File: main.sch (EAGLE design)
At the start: 474 parts, among them J100 DCJ0202, Q200 NMOS, Q201 PMOS, Q300 PMOS, Q400 PMOS, U100 NE555N, U1000 74LS173N, U1001 74LS173N, U1002 74LS245N, U1003 74LS173N, U1004 74LS173N, U1005 74LS245N, U101 NE555N, U102 NE555N, U103 74LS04N, U104 74LS08N, U105 74LS32N, U1100 74LS173N, U1101 74LS173N, U1102 74LS161N, U1106 74HCT154DW, U1107 74HCT154DW, U1108 74LS04N, U1109 74LS04N, U200 HM62256, U201 74LS173N, U202 74LS173N, U203 74LS173N, U204 74LS173N, U205 74LS157N, U206 74LS157N, U207 74LS157N, U208 74LS157N, U209 74HCT595D, U210 74HCT595D, U211 74HCT595D, U212 74LS245N, U213 74LS245N, U214 74LS00N, U215 74LS173N, U216 74LS173N, U217 74LS173N, U218 74LS173N, U219 74LS245N, U220 74LS245N, U300 74LS299N, U301 74LS245N, U302 74LS08N, U303 74LS00N, U304 74LS245N, U400 74LS00N, U401 74LS245N, U500 74LS161N, U501 74LS161N, U502 74LS161N, U503 74LS161N, U504 74LS245N, U505 74LS245N, U600 74LS173N, U601 74LS173N, U602 74LS173N, U603 74LS173N, U604 74LS245N, U700 74LS283N, U701 74LS283N, U702 74LS245N, U703 74LS86N, U704 74LS86N, U705 74LS85N, U706 74LS85N, U707 74LS173N, U708 74LS125N, U800 74LS04N, U801 74LS04N, U802 74LS08N, U803 74LS08N, U804 74LS32N, U805 74LS32N, U806 74LS86N, U807 74LS86N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

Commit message: Routing and layout done.
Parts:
- removed C1109: 0.1µF, rcl:C-EUC0805K
- removed U1109: 74LS04N, 74xx-us:74LS04N
- added C709: 0.1µF, rcl:C-EUC0805K
- added J400: 90152-12, 8BitCpuParts:90152-12
- added LED401: (no value), led:LEDCHIP-LED0805
- added Q401, Q402: NMOS, ExtraParts:SOT23-N-MOSFET
- added R1103: 330Ω?, resistor:R-US_R0805
- added R403: 10kΩ, resistor:R-US_R0805
- added R404: 1kΩ, resistor:R-US_R0805
- added S402: NK236H, 8BitCpuParts:NK236H
- added U709: 74LS153N, 74xx-us:74LS153N
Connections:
- net CMP_= renamed CMP_EQ_INT
- removed net CMP_<: U706A.A<B_O, U707A.D1
- removed net CMP_>: U706A.A>B_O, U707A.D3
- removed net CTRL_15: LED1164.A, XU1105A.D7
- removed net OUT_15: U1108D.O
- new net CMP_GT_INT: U707A.D3, U709A.2Y
- new net CMP_GT_PRE: U706A.A>B_O, U709A.1C3, U709A.2C0, U709A.2C1, U709A.2C2
- new net CMP_LT_INT: U707A.D1, U709A.1Y
- new net CMP_LT_PRE: U706A.A<B_O, U709A.1C0, U709A.1C1, U709A.1C2, U709A.2C3
- new net CPTC: LED1153.A, U709A.B, XU1104A.D4
- new net INPUT_GND: Q401.D, S400.10, S400.11, S400.12, S400.13, S400.14, S400.15, S400.16, S400.9
- new net INPUT_GND_INT: Q401.S, Q402.D
- new net INPUT_LOCK_ARDUINO: A200.A4, Q401.G, R403.1
- new net INPUT_LOCK_EXT: LED401.C, Q402.G, S402.P
- new net LED401_VCC: LED401.A, R404.2
- net !CLK: now also U800F.O
- net !CMP: now also U800A.O; no longer U1109A.O
- net !FE: now also U1108E.O; no longer U1109B.O
- net !NO: now also A200.D8, J400.3
- net !OUT_15: no longer U1108D.I
- net !RM: now also U1108C.O; no longer U1109C.O
- net !RMSB: now also U1108D.O; no longer U1109D.O
- net !RO: now also U1108F.I; no longer U1108C.I
- net BITWISE_XOR_7: now also U709A.A
- net CLK: now also U800F.I
- net CMP: now also U800A.I; no longer U1109A.I
- net FE: now also LED1154.A, U1108E.I, XU1104A.D5; no longer LED1153.A, U1109B.I, XU1104A.D4
- net GND: now also C709.2, J400.1, Q402.S, R1103.2, S402.S, U709A.1G, U709A.2G; no longer C1109.2, S400.10, S400.11, S400.12, S400.13, S400.14, S400.15, S400.16, S400.9
- net HLT: now also LED1155.A, XU1104A.D6; no longer LED1154.A, XU1104A.D5
- net INPUT_0: now also A200.D9, J400.5
- net INPUT_1: now also A200.D10, J400.7
- net INPUT_2: now also A200.D11, J400.9
- net INPUT_3: now also A200.D12, J400.11
- net INPUT_4: now also A200.A0, J400.6
- net INPUT_5: now also A200.A1, J400.8
- net INPUT_6: now also A200.A2, J400.10
- net INPUT_7: now also A200.A3, J400.12
- net LED1107_GND: now also R1100.1; no longer RN1100.R8_1
- net LED1108_GND: now also R1101.1; no longer R1100.1
- net LED1109_GND: now also R1102.1; no longer R1101.1
- net LED1110_GND: now also R1103.1; no longer R1102.1
- net LED1111_GND: now also RN1101.R8_1; no longer RN1101.R1_1
- net LED1112_GND: now also RN1101.R7_1; no longer RN1101.R2_1
- net LED1113_GND: now also RN1101.R6_1; no longer RN1101.R3_1
- net LED1114_GND: now also RN1101.R5_1; no longer RN1101.R4_1
- net LED1115_GND: now also RN1101.R4_1; no longer RN1101.R5_1
- net LED1116_GND: now also RN1101.R3_1; no longer RN1101.R6_1
- net LED1117_GND: now also RN1101.R2_1; no longer RN1101.R7_1
- net LED1118_GND: now also RN1101.R1_1; no longer RN1101.R8_1
- net LED1134_VCC: now also RN1104.R7_1; no longer RN1104.R2_1
- net LED1135_VCC: now also RN1104.R6_1; no longer RN1104.R3_1
- net LED1136_VCC: now also RN1104.R5_1; no longer RN1104.R4_1
- net LED1137_VCC: now also RN1104.R4_1; no longer RN1104.R5_1
- net LED1138_VCC: now also RN1104.R3_1; no longer RN1104.R6_1
- net LED1139_VCC: now also RN1104.R2_1; no longer RN1104.R7_1
- net LED1140_VCC: now also RN1104.R1_1; no longer RN1104.R8_1
- net LED1141_VCC: now also RN1105.R8_1; no longer RN1105.R1_1
- net LED1142_VCC: now also RN1105.R7_1; no longer RN1105.R2_1
- net LED1143_VCC: now also RN1105.R6_1; no longer RN1105.R3_1
- net LED1144_VCC: now also RN1105.R5_1; no longer RN1105.R4_1
- net LED1145_VCC: now also RN1105.R4_1; no longer RN1105.R5_1
- net LED1146_VCC: now also RN1105.R3_1; no longer RN1105.R6_1
- net LED1147_VCC: now also RN1105.R2_1; no longer RN1105.R7_1
- net LED1148_VCC: now also RN1105.R1_1; no longer RN1105.R8_1
- net LED1149_GND: now also RN1106.R8_1; no longer RN1106.R1_1
- net LED1150_GND: now also RN1106.R7_1; no longer RN1106.R2_1
- net LED1151_GND: now also RN1106.R6_1; no longer RN1106.R3_1
- net LED1152_GND: now also RN1106.R5_1; no longer RN1106.R4_1
- net LED1153_GND: now also RN1106.R4_1; no longer RN1106.R5_1
- net LED1154_GND: now also RN1106.R3_1; no longer RN1106.R6_1
- net LED1155_GND: now also RN1106.R2_1; no longer RN1106.R7_1
- net LED1156_GND: now also RN1106.R1_1; no longer RN1106.R8_1
- net LED1157_GND: now also RN1107.R8_1; no longer RN1107.R1_1
- net LED1158_GND: now also RN1107.R7_1; no longer RN1107.R2_1
- net LED1159_GND: now also RN1107.R6_1; no longer RN1107.R3_1
- net LED1160_GND: now also RN1107.R5_1; no longer RN1107.R4_1
- net LED1161_GND: now also RN1107.R4_1; no longer RN1107.R5_1
- net LED1162_GND: now also RN1107.R3_1; no longer RN1107.R6_1
- net LED1163_GND: now also RN1107.R2_1; no longer RN1107.R7_1
- net LED1164_GND: now also RN1107.R1_1; no longer RN1107.R8_1
- net NO_RESET_PULSE: now also A200.D7, J400.4
- net RM: now also LED1156.A, U1108C.I, XU1104A.D7; no longer LED1155.A, U1109C.I, XU1104A.D6
- net RMSB: now also LED1157.A, U1108D.I, XU1105A.D0; no longer LED1156.A, U1109D.I, XU1104A.D7
- net RO: now also U1108F.O; no longer U1108C.O
- net SM0: now also LED1158.A, XU1105A.D1; no longer LED1157.A, XU1105A.D0
- net SM1: now also LED1159.A, XU1105A.D2; no longer LED1158.A, XU1105A.D1
- net SRO: now also LED1160.A, XU1105A.D3; no longer LED1159.A, XU1105A.D2
- net SUB: now also LED1161.A, XU1105A.D4; no longer LED1160.A, XU1105A.D3
- net T0: now also LED1162.A, XU1105A.D5; no longer LED1161.A, XU1105A.D4
- net T1: now also LED1163.A, XU1105A.D6; no longer LED1162.A, XU1105A.D5
- net VCC: now also C709.1, J400.2, R403.2, R404.1, S402.O; no longer C1109.1
- net XR: now also LED1164.A, XU1105A.D7; no longer LED1163.A, XU1105A.D6

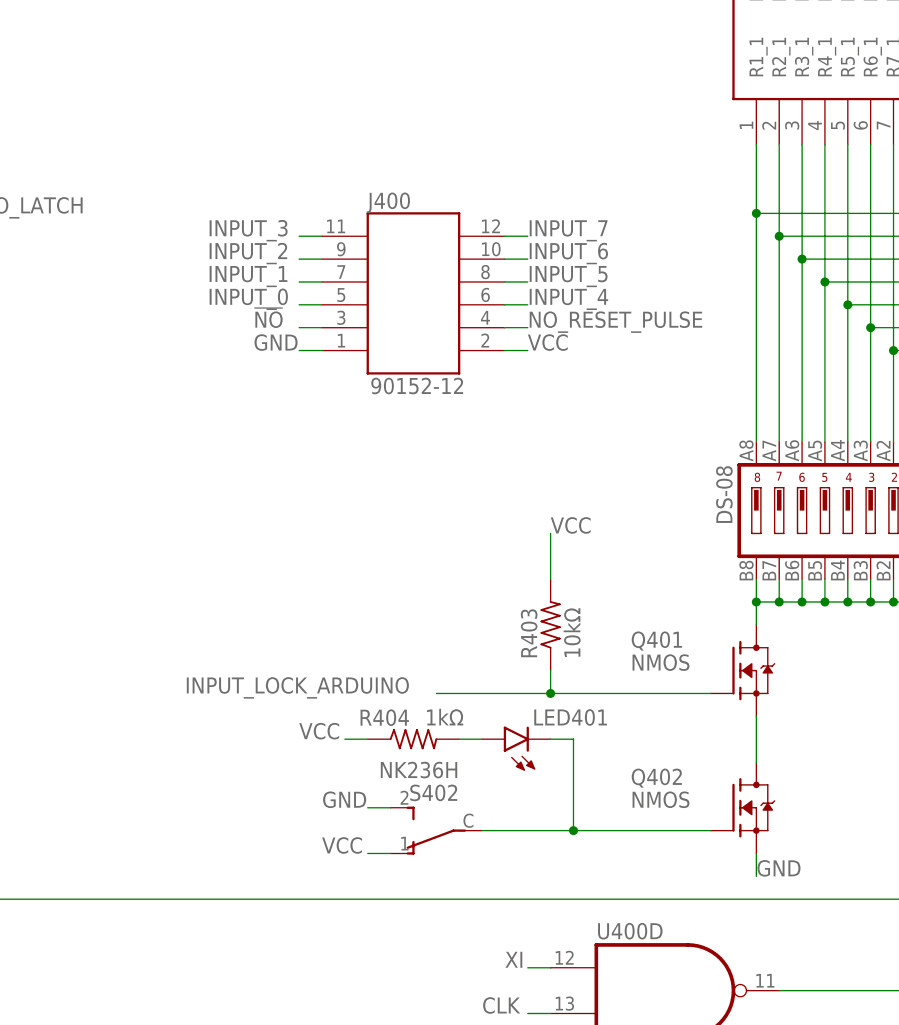
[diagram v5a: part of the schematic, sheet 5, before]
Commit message: Revised external input, progress on silkscreen.
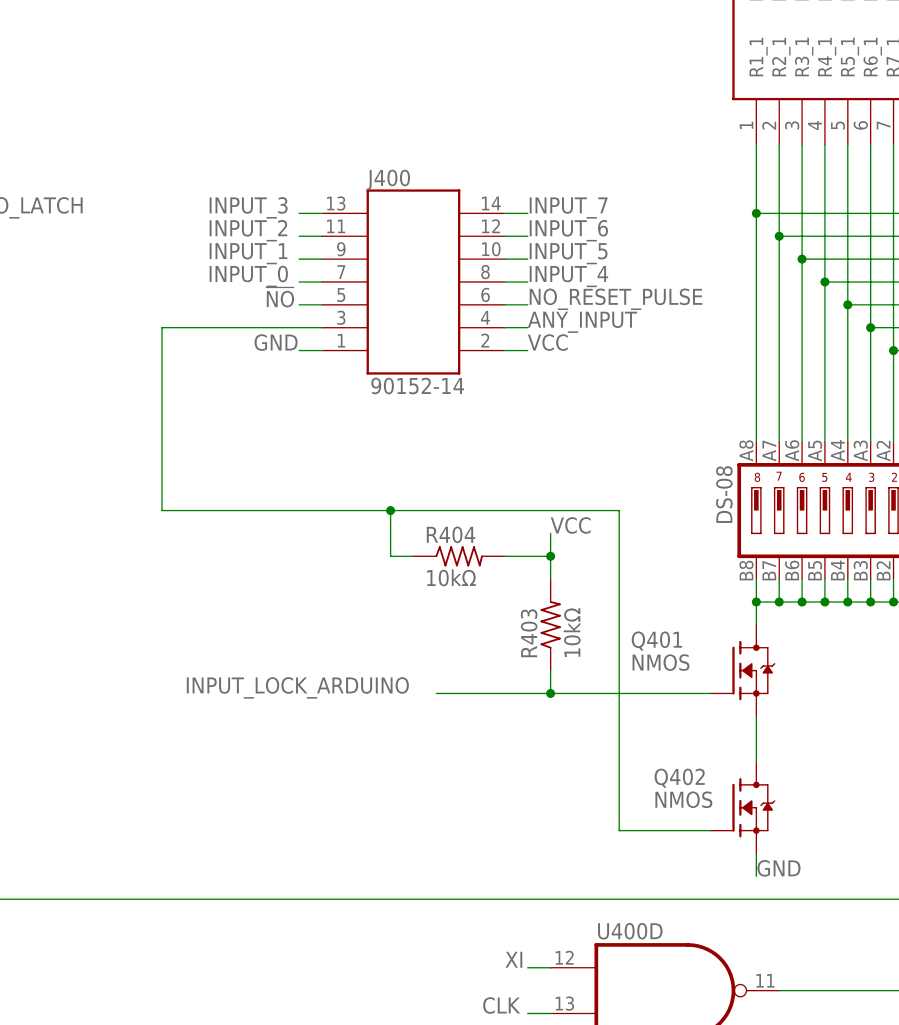
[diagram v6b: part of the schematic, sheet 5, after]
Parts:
- removed LED401: (no value), led:LEDCHIP-LED0805
- removed S402: NK236H, 8BitCpuParts:NK236H
- J400: value 90152-12 -> 90152-14; device 8BitCpuParts:90152-12 -> 8BitCpuParts:90152-14
- R404: value 1kΩ -> 10kΩ
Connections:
- removed net LED401_VCC: LED401.A, R404.2
- new net ANY_INPUT: A200.A5, J400.4, U1106A.0
- net !NO: now also J400.5; no longer J400.3
- net GND: no longer S402.S
- net INPUT_0: now also J400.7; no longer J400.5
- net INPUT_1: now also J400.9; no longer J400.7
- net INPUT_2: now also J400.11; no longer J400.9
- net INPUT_3: now also J400.13; no longer J400.11
- net INPUT_4: now also J400.8; no longer J400.6
- net INPUT_5: now also J400.10; no longer J400.8
- net INPUT_6: now also J400.12; no longer J400.10
- net INPUT_7: now also J400.14; no longer J400.12
- net INPUT_LOCK_EXT: now also J400.3, R404.1; no longer LED401.C, S402.P
- net NO_RESET_PULSE: now also J400.6; no longer J400.4
- net VCC: now also R404.2; no longer R404.1, S402.O
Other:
- moved on the sheet: R404

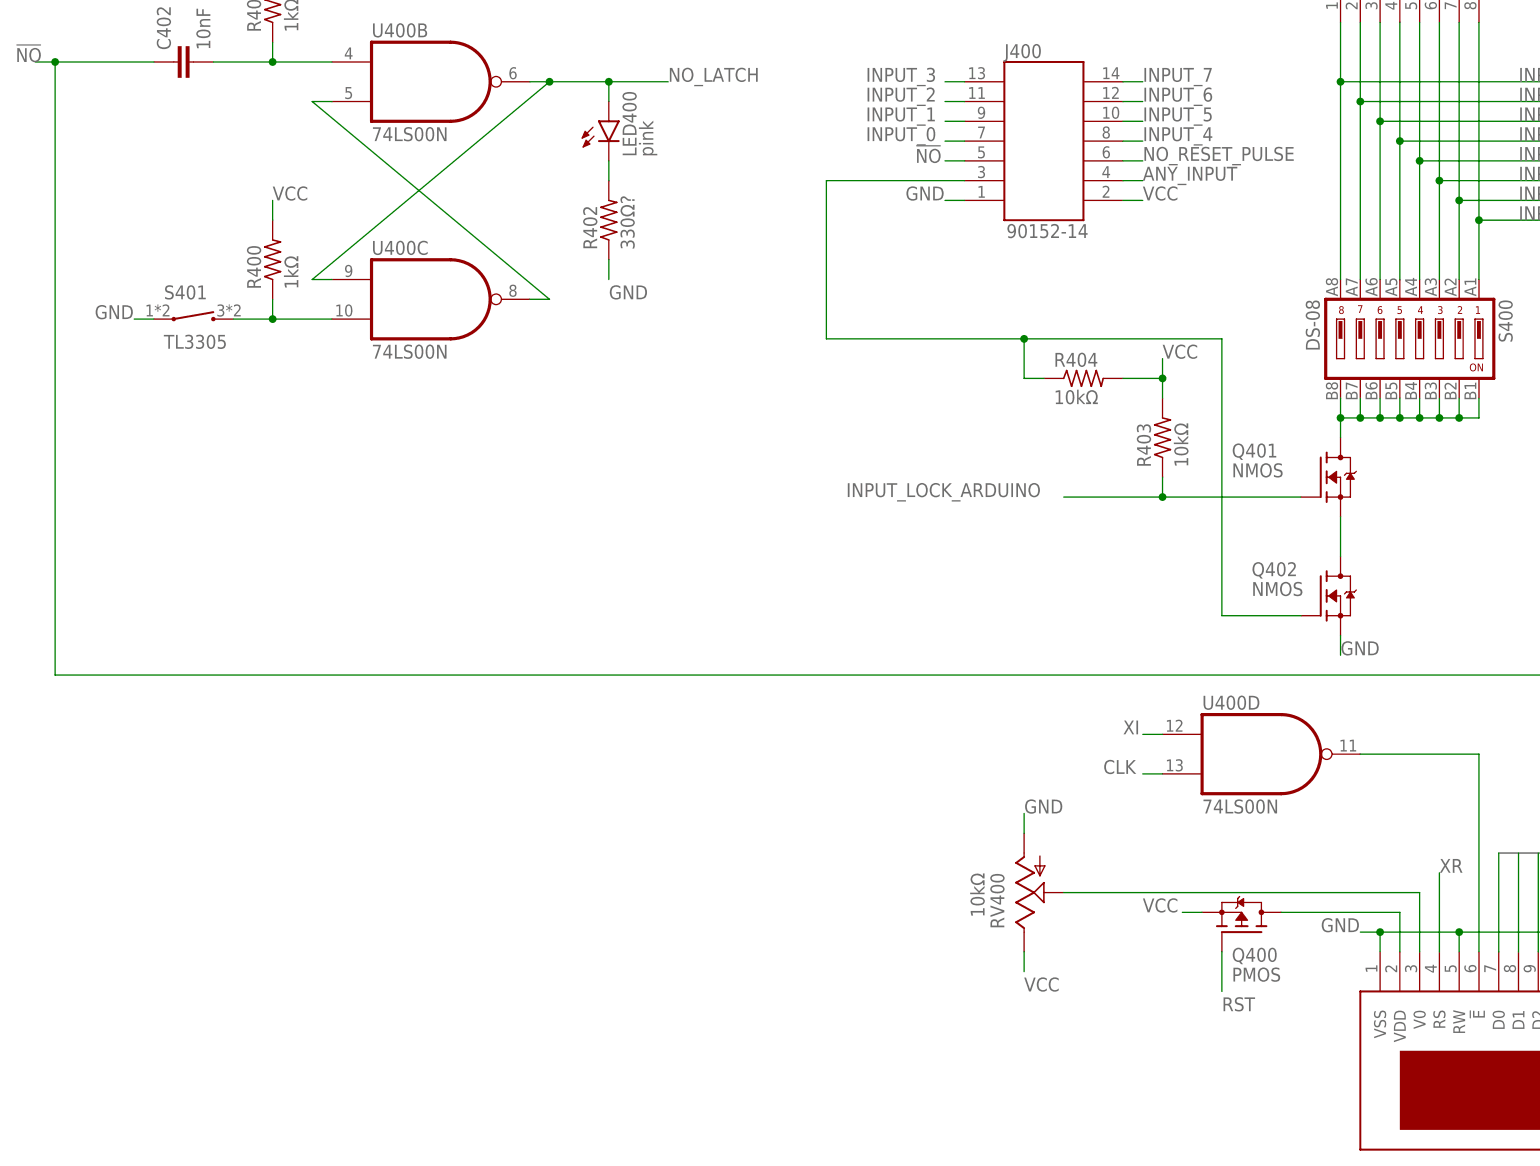
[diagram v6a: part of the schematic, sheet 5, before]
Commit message: Fixed issues encountered during build and testing.
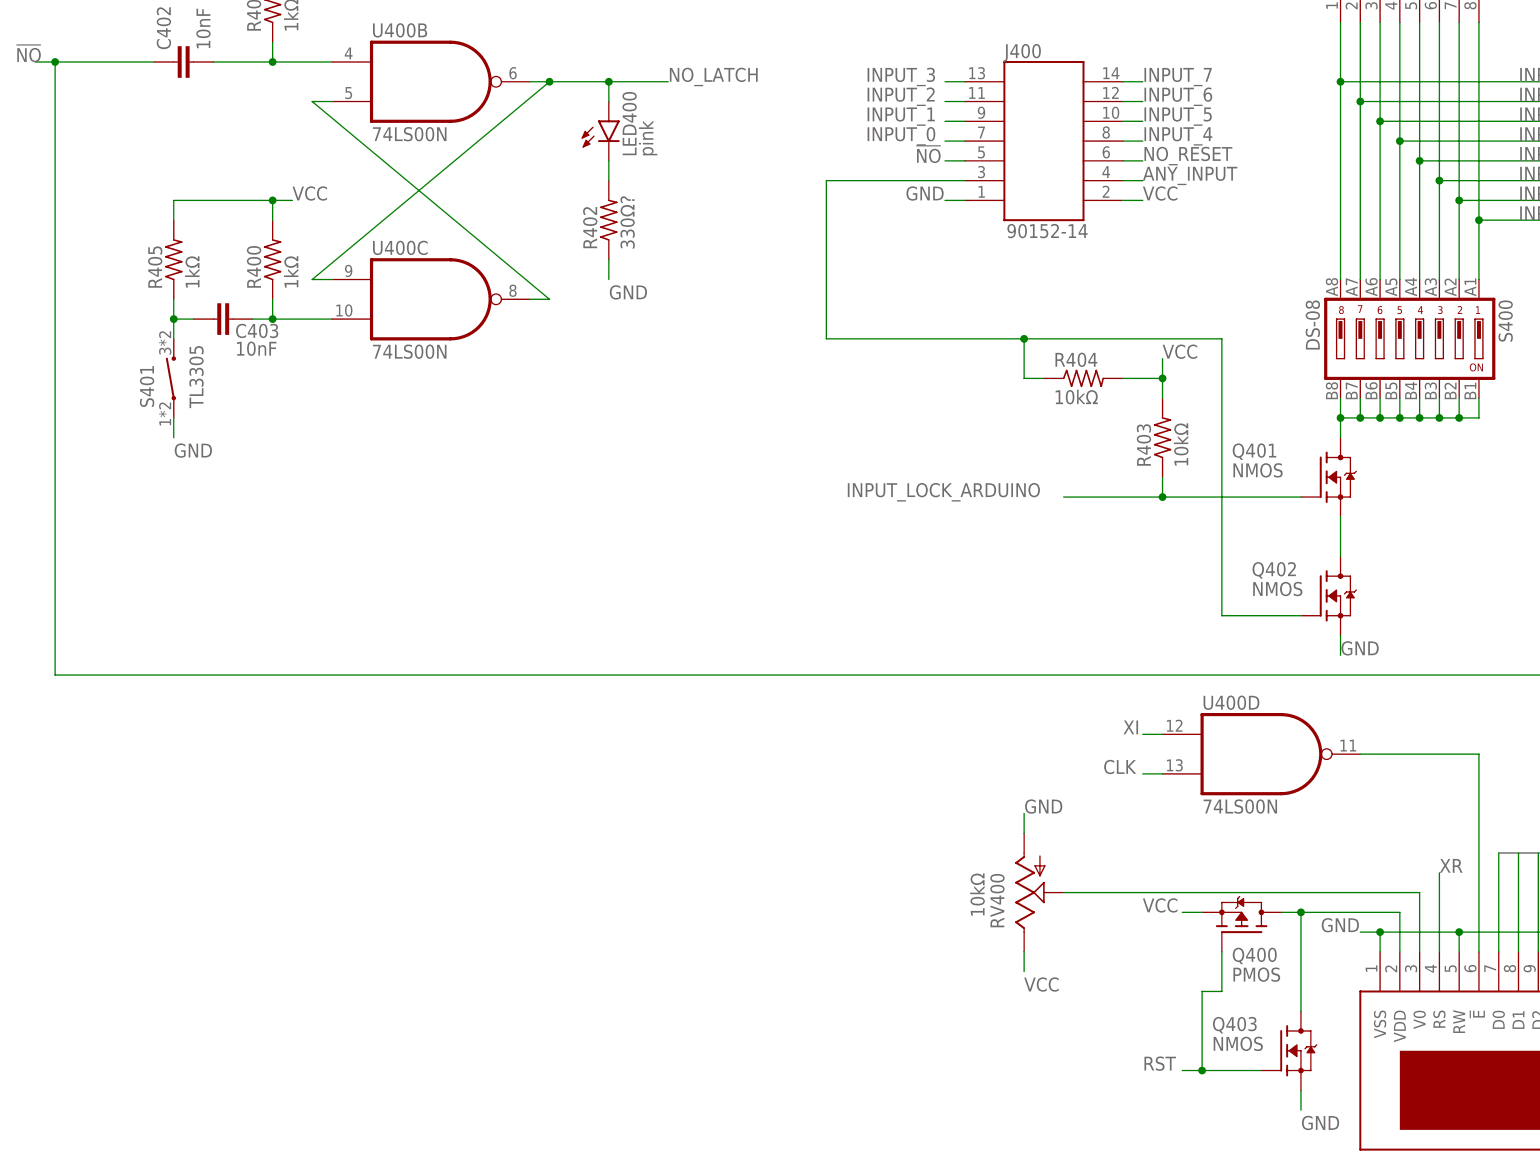
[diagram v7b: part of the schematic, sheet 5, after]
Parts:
- added C1109, C1110: 0.1µF, rcl:C-EUC0805K
- added C403: 10nF, rcl:C-EUC0805K
- added Q403: NMOS, ExtraParts:SOT23-N-MOSFET
- added R405: 1kΩ, resistor:R-US_R0805
- R100, R101: value 330Ω -> 150Ω
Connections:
- new net ARDUINO_DETECT_GND: A200.GND1, Q200.G, R200.1, U209A.G, U210A.G, U211A.G
- new net MEM_!OE_INT: U103D.O, U105A.I0
- new net NO_RESET: A200.D7, C403.1, J400.6, R405.1, S401.2
- net GND: now also A200.GND2, C1109.2, C1110.2, Q403.S; no longer A200.GND, Q200.G, R200.1, U209A.G, U210A.G, U211A.G
- net LCD_VDD: now also Q403.D
- net MEM_!OE: now also U105A.O; no longer U103D.O
- net NO_RESET_PULSE: now also C403.2; no longer A200.D7, J400.6, S401.2
- net RI: now also U105A.I1
- net RM: now also C1109.1
- net RMSB: now also C1110.1
- net RST: now also Q403.G
- net VCC: now also R405.2
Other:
- note removed: "Connect GND to one Arduino GND pin, and !G + Q200 to the other Arduino GND pin (Arduino detection)"
- moved on the sheet: S401, U103D

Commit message: Moved library over to central BW lib, added gitignore
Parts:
- A200: device 8BitCpuParts:ARDUINO_NANO_V3 -> BW-Active:ARDUINO_NANO_V3
- DS400: device 8BitCpuParts:HD44780_LCD -> BW-Active:HD44780_LCD
- DS900, DS901, DS902, DS903: device 8BitCpuParts:LED_7SEG_CC -> BW-Active:LED_7SEG_CC
- J400: device 8BitCpuParts:90152-14 -> BW-Connectors:90152-14
- Q200, Q401, Q402, Q403: device ExtraParts:SOT23-N-MOSFET -> BW-Active:SOT23-N-MOSFET
- Q201, Q300, Q400: device ExtraParts:SOT23-P-MOSFET -> BW-Active:SOT23-P-MOSFET
- RN1000, RN1001, RN1100, RN1101, RN1102, RN1103, RN1104, RN1105, RN1106, RN1107, RN200, RN201, RN202, RN203, RN204, RN205, RN206, RN207, RN300, RN301, RN302, RN400, RN500, RN501, RN600, RN601, RN700, RN800, RN900: device 8BitCpuParts:CAY16-102J8LF -> BW-PassiveMechanical:CAY16-102J8LF
- S100, S204, S300, S401: device ExtraParts:TL3305 -> BW-PassiveMechanical:TL3305
- S101, S200: device 8BitCpuParts:ESP10 -> BW-PassiveMechanical:ESP10
- S201, S202, S203, S400: device 8BitCpuParts:DS-08 -> BW-PassiveMechanical:DS-08
- U1102, U500, U501, U502, U503, U901: device 8BitCpuParts:74LS161N -> BW-Active:74LS161N
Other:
- moved on the sheet: RN200, RN201, RN202, RN300, RN301, RN400, RN900
